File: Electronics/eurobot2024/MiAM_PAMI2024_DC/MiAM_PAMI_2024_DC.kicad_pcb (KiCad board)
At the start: 2 copper layers, 62 x 95 mm, 30 parts, among them J1 Conn_01x03_Male, J2 Conn_01x03_Male, J3 SSD1306_vertical, Q1 BS170F, SW1 SW_DPDT_x2, U1 ESP32-DEVKITC-32U, U2 3V3, U4 5V, U6 TB6612FNG

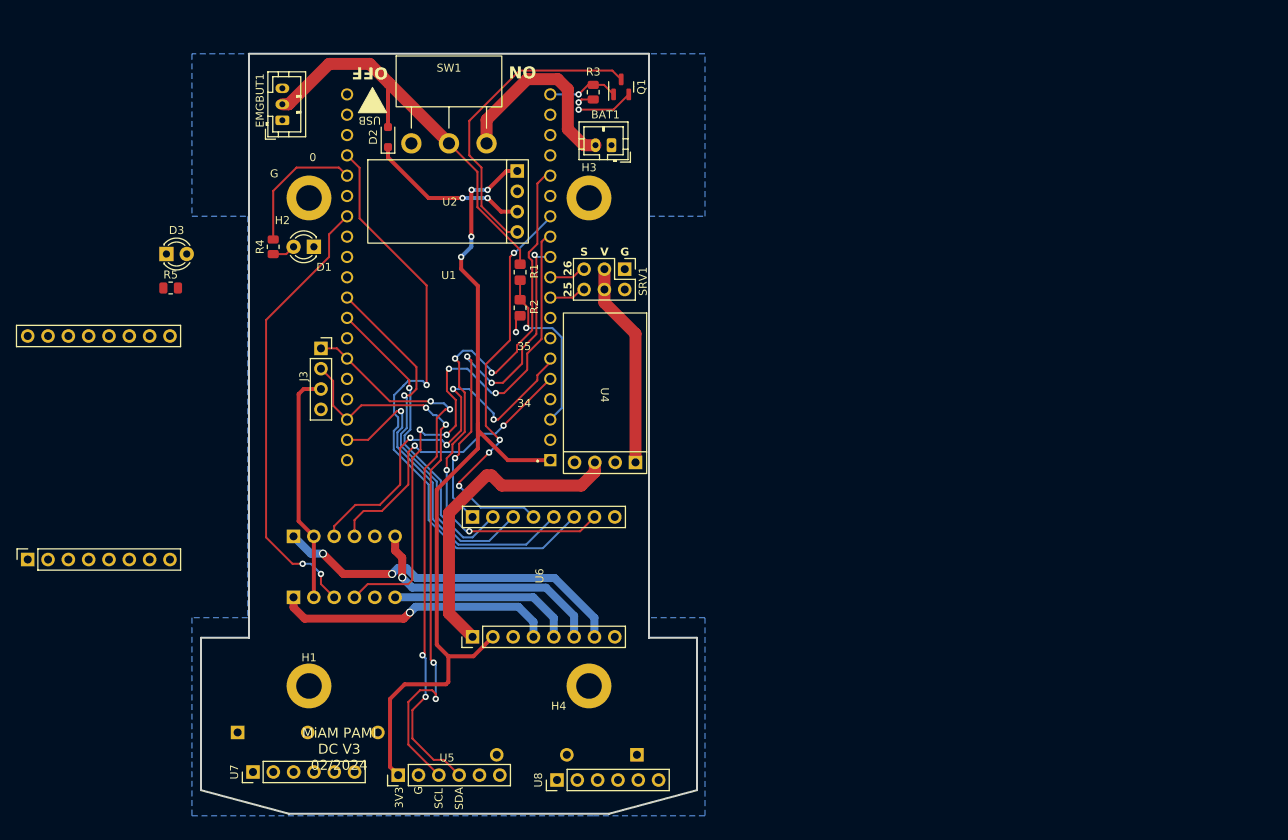
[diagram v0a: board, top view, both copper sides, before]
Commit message: Add new PAMI PCB
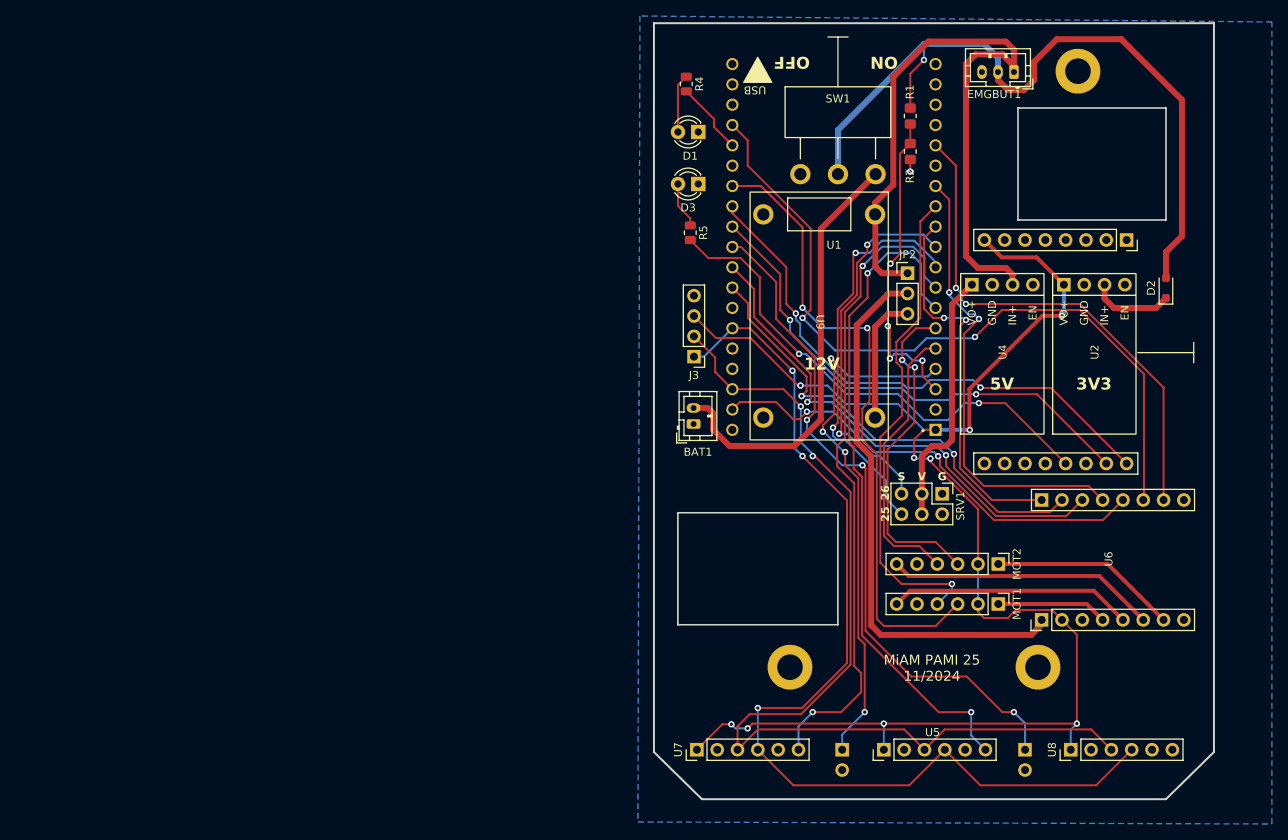
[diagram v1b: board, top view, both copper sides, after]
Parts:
- removed H3: MountingHole_Pad, MountingHole:MountingHole_3.2mm_M3_DIN965_Pad
- removed Q1: BS170F, Package_TO_SOT_SMD:SOT-23
- removed R3: 50k, Resistor_SMD:R_0805_2012Metric
- added JP2: SolderJumper_3_Open, Connector_PinHeader_2.54mm:PinHeader_1x03_P2.54mm_Vertical, F.Cu at (208.2, 73.1)
- added U9: MT3608, MiAM_ESP32_Footprints:MT3608, F.Cu at (197.2, 78.5)
- J1, J2: value Conn_01x03_Male -> Conn_01x02_Pin; footprint MiAM_ESP32_Footprints:Microruptor -> Connector_PinHeader_2.54mm:PinHeader_1x02_P2.54mm_Vertical
- J3: footprint MiAM_ESP32_Footprints:SSD1306_vertical -> Connector_PinHeader_2.54mm:PinHeader_1x04_P2.54mm_Vertical
- MOT1, MOT2: moved to F.Cu
- moved U3 120.4 mm to (226.8, 83.1), turned to -90 degrees
- moved D2 99.1 mm to (240.5, 75.0)
- moved H2 97.4 mm to (229.5, 47.9)
- moved EMGBUT1 91.7 mm to (221.5, 48.0), turned to 180 degrees
- moved MOT2 88.2 mm to (219.5, 109.5)
- moved MOT1 88.1 mm to (219.5, 114.5)
- moved U2 83.3 mm to (231.5, 83.5), turned to 90 degrees
- moved J1 75.6 mm to (200.0, 132.7), turned to 180 degrees
- moved U6 71.2 mm to (245.3, 116.5)
- moved D3 67.1 mm to (182.0, 62.0), turned to 180 degrees
- moved R5 65.3 mm to (181.0, 68.1), turned to -90 degrees
- moved U8 64.3 mm to (228.6, 132.7)
- moved U5 60.8 mm to (205.2, 132.7)
- moved H1 60.2 mm to (193.5, 122.4)
- moved H4 56.2 mm to (224.5, 122.4)
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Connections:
- J1 pad 1: /SW1 -> /SW0
- J2 pad 1: /SW0 -> /SW1
- U2 pad 4: Net-(Q1-D) -> unconnected-(U2-EN-Pad4)
- U6 pad 1: /EMERGENCY_BUTTON -> +12V
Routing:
- net /SW1: track 0.00 -> 85.8 mm, vias 0 -> 3
- net /XSHUT0: track 0.00 -> 84.5 mm, vias 0 -> 2
- net /XSHUT1: track 0.00 -> 81.9 mm, vias 0 -> 2
- net +12V: track 0.00 -> 69.2 mm
- net /RX2: track 0.00 -> 67.9 mm, vias 0 -> 2
- net /SW0: track 0.00 -> 67.6 mm, vias 0 -> 4
- net /TX2: track 0.00 -> 63.1 mm, vias 0 -> 2
- net /BW23: track 0.00 -> 63.0 mm, vias 0 -> 2
- net /SDA: track 70.8 -> 128.1 mm, vias 4 -> 3
- net /SCL: track 72.7 -> 124.2 mm, vias 4 -> 2
- net +3V3: track 137.7 -> 187.9 mm, vias 4 -> 9
- net /EMERGENCY_BUTTON: track 39.3 -> 89.1 mm
- net /SERVO_PWM_1: track 4.27 -> 50.4 mm, vias 0 -> 2
- net /POWER_SWITCH: track 51.4 -> 95.8 mm, vias 0 -> 1
- net /SERVO_PWM_2: track 4.27 -> 46.9 mm, vias 0 -> 2
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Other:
- board size 62 x 95 mm -> 70 x 97 mm
- board text added: "12V"
- board text added: "5V"
- board text added: "Component exclusion zone"
- board text added: "MiAM PAMI 25 11/2024"
- board text removed: "0"
- board text removed: "34"
- board text removed: "35"
- board text removed: "MiAM PAMI DC V3 02/2024"
- board text removed: "SCL"
- board text removed: "SDA"

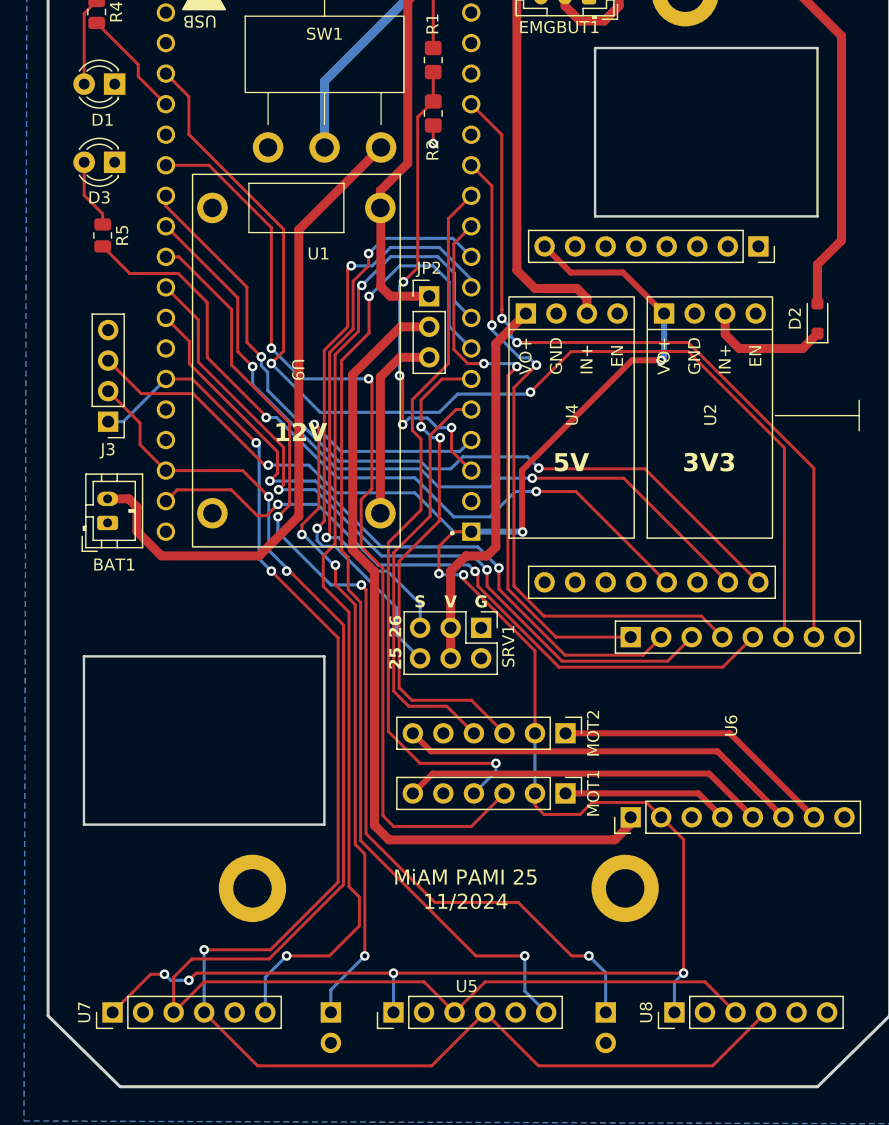
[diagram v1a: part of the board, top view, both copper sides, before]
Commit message: Add LED ring and better routing
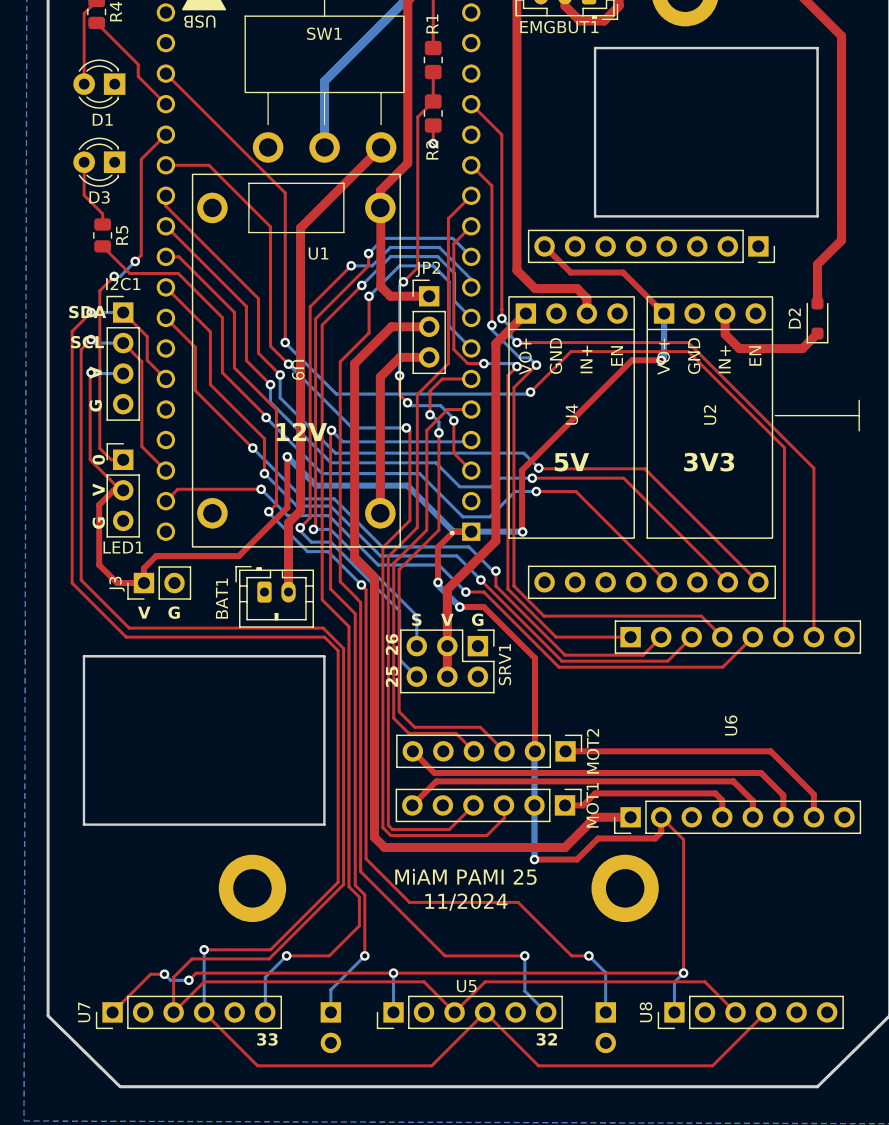
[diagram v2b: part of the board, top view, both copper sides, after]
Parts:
- added I2C1: SSD1306_vertical, Connector_PinHeader_2.54mm:PinHeader_1x04_P2.54mm_Vertical, F.Cu at (182.8, 74.5)
- added LED1: Conn_01x03_Pin, Connector_PinHeader_2.54mm:PinHeader_1x03_P2.54mm_Vertical, F.Cu at (182.8, 86.8)
- J3: value SSD1306_vertical -> Conn_01x02_Pin; footprint Connector_PinHeader_2.54mm:PinHeader_1x04_P2.54mm_Vertical -> Connector_PinHeader_2.54mm:PinHeader_1x02_P2.54mm_Vertical
- moved BAT1 14.3 mm to (194.5, 97.8), turned to 0 degrees
- moved J3 13.7 mm to (184.5, 97.0), turned to 90 degrees
- moved SRV1 1.55 mm to (212.2, 102.2)
- moved MOT2 1.50 mm to (219.5, 111.0)
- moved MOT1 1.00 mm to (219.5, 115.5)
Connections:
- net /BW23 renamed /LED_BW16
- net /GPIO2 renamed /LED_ESP32
- J3 pad 1: /SDA -> +3V3
- J3 pad 2: /SCL -> GND
- U1 pad 25: unconnected-(U1-IO0-Pad25) -> /LED_RING
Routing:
- net +3V3: track 187.9 -> 220.4 mm, vias 9 -> 11
- net /LED_RING: track 0.00 -> 31.0 mm, vias 0 -> 2
- net /SCL: track 124.2 -> 150.2 mm, vias 2 -> 1
- net /SDA: track 128.1 -> 149.3 mm, vias 3 -> 2
- net /BATTERY_INPUT: track 53.9 -> 40.2 mm
- net /SW0: track 67.6 -> 62.9 mm, vias 4 -> 2
- net /4A: track 94.1 -> 90.4 mm
- net /SERVO_PWM_1: track 50.4 -> 53.3 mm
- net /ENCODER_A2: track 35.0 -> 37.3 mm
- net /ENCODER_A1: track 61.3 -> 63.3 mm, vias 1 -> 0
- net /ENCODER_B1: track 79.3 -> 81.2 mm
- net /SERVO_PWM_2: track 46.9 -> 48.6 mm
- net /XSHUT0: track 84.5 -> 86.1 mm
- net /2A: track 57.9 -> 56.3 mm
- net /3A: track 57.7 -> 56.4 mm
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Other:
- board text added: "0"
- board text added: "32"
- board text added: "33"
- board text added: "SCL"
- board text added: "SDA"

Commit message: Fix PAMI pcb
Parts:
- added G***: LOGO, MiAM_ESP32_Footprints:miam_logo, F.Cu at (211.3, 123.7)
- D1, D3: footprint LED_THT:LED_D3.0mm -> LED_SMD:LED_0805_2012Metric
- JP2: footprint Connector_PinHeader_2.54mm:PinHeader_1x03_P2.54mm_Vertical -> Jumper:SolderJumper-3_P1.3mm_Bridged12_Pad1.0x1.5mm_NumberLabels
- R4: value 200 -> 1K
- R5: value 200 -> 5K
- moved D1 7.19 mm to (180.7, 48.4), turned to -90 degrees
- moved R4 4.59 mm to (180.7, 54.1)
- moved J3 2.55 mm to (187.0, 97.0)
- moved U6 2.52 mm to (242.9, 115.6)
- moved JP2 2.26 mm to (208.0, 75.4), turned to -90 degrees
- moved BAT1 2.00 mm to (196.5, 97.7), turned to 180 degrees
- moved SRV1 1.90 mm to (214.1, 101.9)
- moved LED1 1.50 mm to (182.2, 88.2)
- moved D3 1.07 mm to (181.0, 62.2), turned to -90 degrees
- moved MOT1 0.76 mm to (218.8, 115.4)
- moved MOT2 0.76 mm to (218.8, 110.9)
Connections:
- LED1 pad 1: /LED_RING -> +3V3
- LED1 pad 2: +3V3 -> /LED_RING
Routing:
- net /4A: track 90.4 -> 81.3 mm
- net /EN34: track 64.5 -> 57.8 mm
- net /EN12: track 47.4 -> 41.1 mm, vias 2 -> 1
- net /STBY: track 57.6 -> 53.2 mm, vias 2 -> 1
- net GND: track 1.51 -> 5.78 mm, vias 1 -> 3
- net /LED_RING: track 31.0 -> 34.7 mm
- net Net-(D1-A): track 7.34 -> 3.80 mm
- net /ENCODER_B2: track 42.4 -> 39.0 mm
- net /LED_ESP32: track 9.14 -> 6.50 mm
- net /ENCODER_A2: track 37.3 -> 34.8 mm
- net /3Y: track 24.0 -> 22.0 mm
- net /1Y: track 15.1 -> 13.1 mm
- net /2Y: track 31.2 -> 29.2 mm
- net /4Y: track 34.2 -> 32.2 mm
- net /SCL: track 150.2 -> 152.1 mm
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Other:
- board size 70 x 97 mm -> 69.8 x 96.8 mm
- board text added: "BW16"
- board text added: "ESP32"

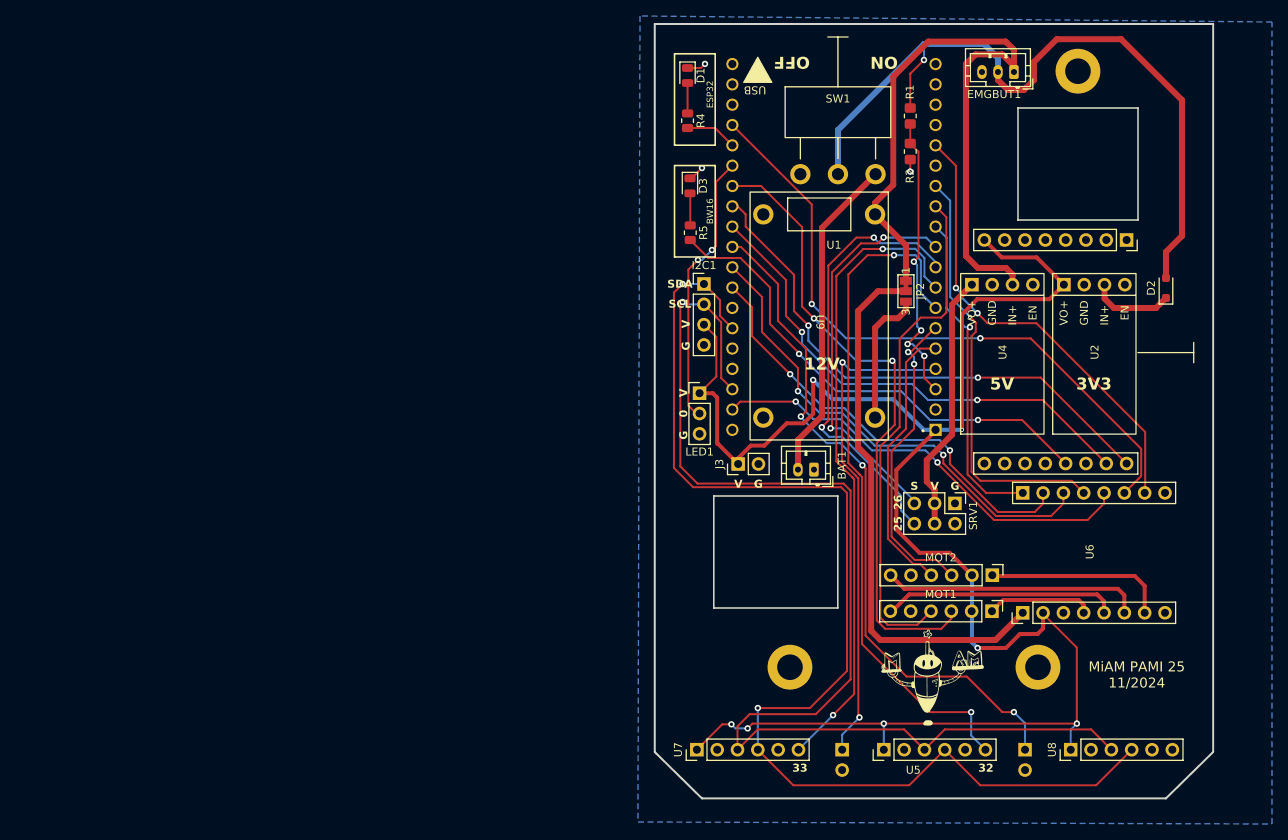
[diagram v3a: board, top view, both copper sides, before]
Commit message: Add additional breakout for BW16
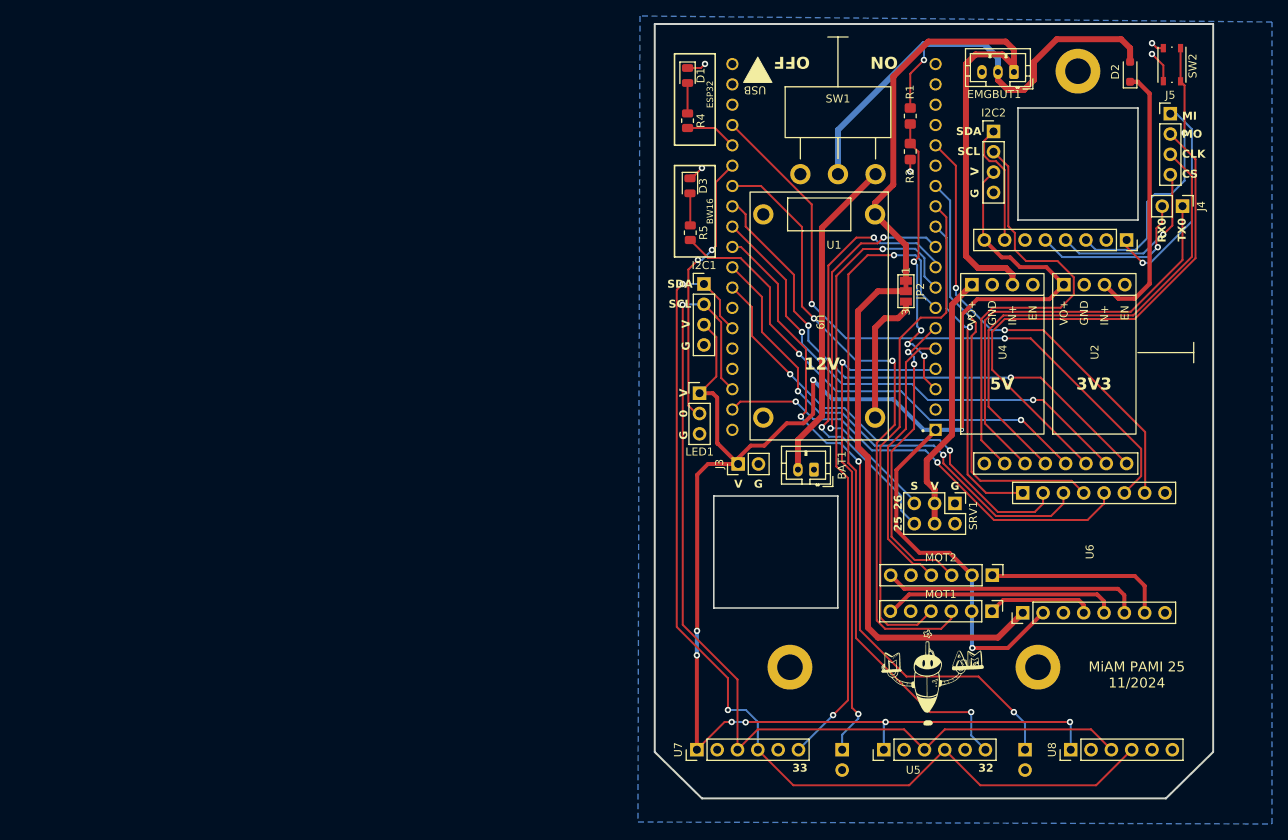
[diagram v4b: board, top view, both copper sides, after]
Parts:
- added I2C2: SSD1306_vertical, Connector_PinHeader_2.54mm:PinHeader_1x04_P2.54mm_Vertical, F.Cu at (218.9, 55.4)
- added J4: Conn_01x02_Pin, Connector_PinHeader_2.54mm:PinHeader_1x02_P2.54mm_Vertical, F.Cu at (242.6, 64.8)
- added J5: Conn_01x04_Pin, Connector_PinHeader_2.54mm:PinHeader_1x04_P2.54mm_Vertical, F.Cu at (241.0, 53.2)
- added SW2: SW_Push, Button_Switch_SMD:SW_Push_1P1T_NO_Vertical_Wuerth_434133025816, F.Cu at (241.2, 47.1)
- moved D2 27.4 mm to (236.0, 48.0)
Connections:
- U3 pad 1: unconnected-(U3-20-Pad1) -> /MISO_BW16
- U3 pad 10: unconnected-(U3-16-Pad10) -> /SCL_BW16
- U3 pad 11: unconnected-(U3-14_TX0-Pad11) -> /TX0_BW16
- U3 pad 12: unconnected-(U3-19-Pad12) -> /CLK_BW16
- U3 pad 14: unconnected-(U3-21-Pad14) -> /MOSI_BW16
- U3 pad 3: unconnected-(U3-EN-Pad3) -> /EN_BW16
- U3 pad 4: unconnected-(U3-18-Pad4) -> /CS_BW16
- U3 pad 5: unconnected-(U3-15_RX0-Pad5) -> /RX0_BW16
- U3 pad 7: unconnected-(U3-17-Pad7) -> /SDA_BW16
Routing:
- net /MOSI_BW16: track 0.00 -> 67.2 mm
- net /CLK_BW16: track 0.00 -> 62.6 mm
- net /SCL_BW16: track 0.00 -> 56.4 mm
- net /TX0_BW16: track 0.00 -> 54.5 mm
- net /EN_BW16: track 0.00 -> 35.9 mm, vias 0 -> 1
- net +3V3: track 219.3 -> 251.1 mm, vias 7 -> 9
- net /POWER_SWITCH: track 95.8 -> 65.3 mm
- net /SCL: track 152.1 -> 124.2 mm
- net /MISO_BW16: track 0.00 -> 27.0 mm, vias 0 -> 1
- net Net-(D2-K): track 10.4 -> 33.9 mm
- net /SDA: track 150.7 -> 127.8 mm
- net /CS_BW16: track 0.00 -> 21.9 mm, vias 0 -> 1
- net /RX0_BW16: track 0.00 -> 21.0 mm, vias 0 -> 1
- net /SDA_BW16: track 0.00 -> 15.6 mm
- net GND: track 5.78 -> 11.4 mm, vias 3 -> 5
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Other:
- board text added: "CLK"
- board text added: "CS"
- board text added: "MI"
- board text added: "MO"
- board text added: "RX0"
- board text added: "TX0"

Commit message: Update PCB
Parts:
- moved EMGBUT1 3.91 mm to (217.6, 47.8), turned to 0 degrees
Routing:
- net /EMERGENCY_BUTTON: track 88.0 -> 75.7 mm
